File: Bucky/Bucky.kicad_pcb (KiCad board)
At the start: 2 copper layers, 75 x 44.5 mm, 27 parts, among them J1 XT60PW-M, J10 XT30AW-M, J11 XT30AW-M, J12 XT30AW-M, J13 XT30AW-M, J14 XT30AW-M, J2 XT60PW-M, J3 XT30PW-M, J4 XT30PW-M, J5 XT30PW-M, J6 XT30PW-M, J7 XT30AW-M, J8 XT30AW-M, J9 XT30AW-M

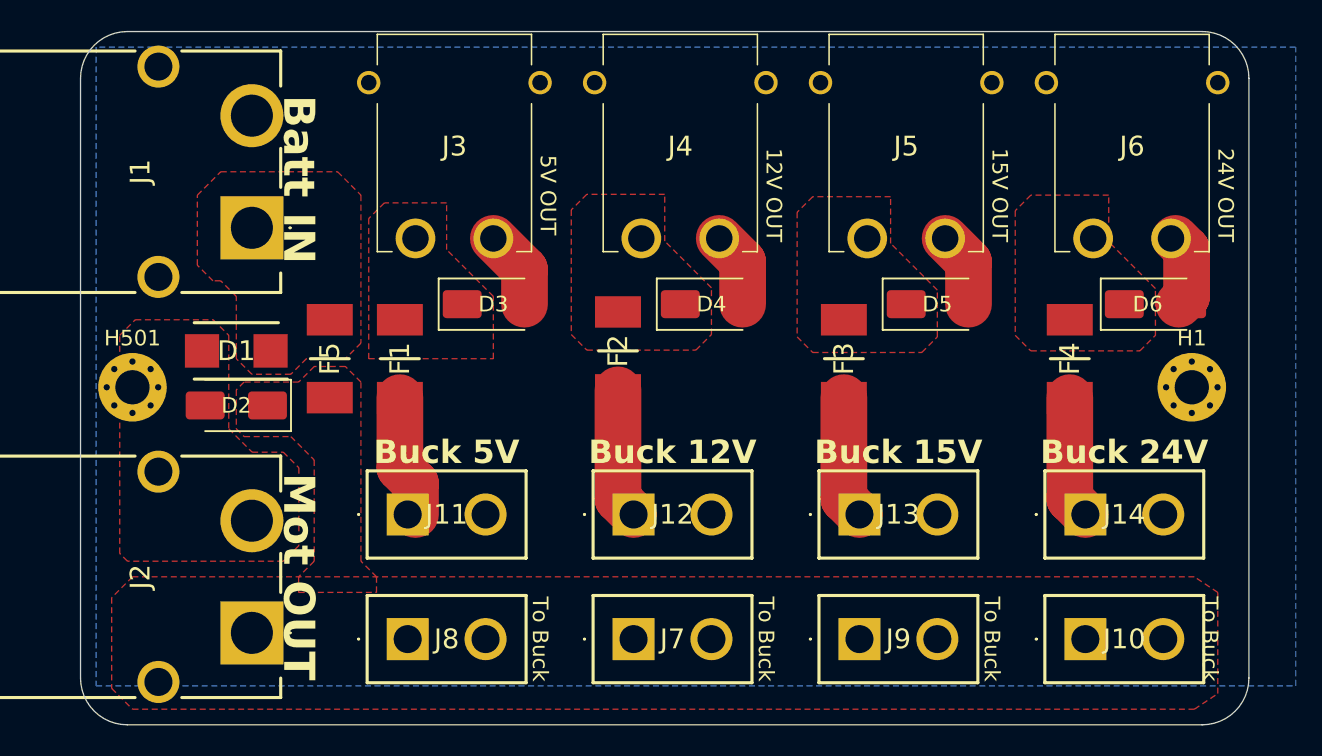
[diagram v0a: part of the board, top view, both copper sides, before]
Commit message: fixed xt60 polarity connection
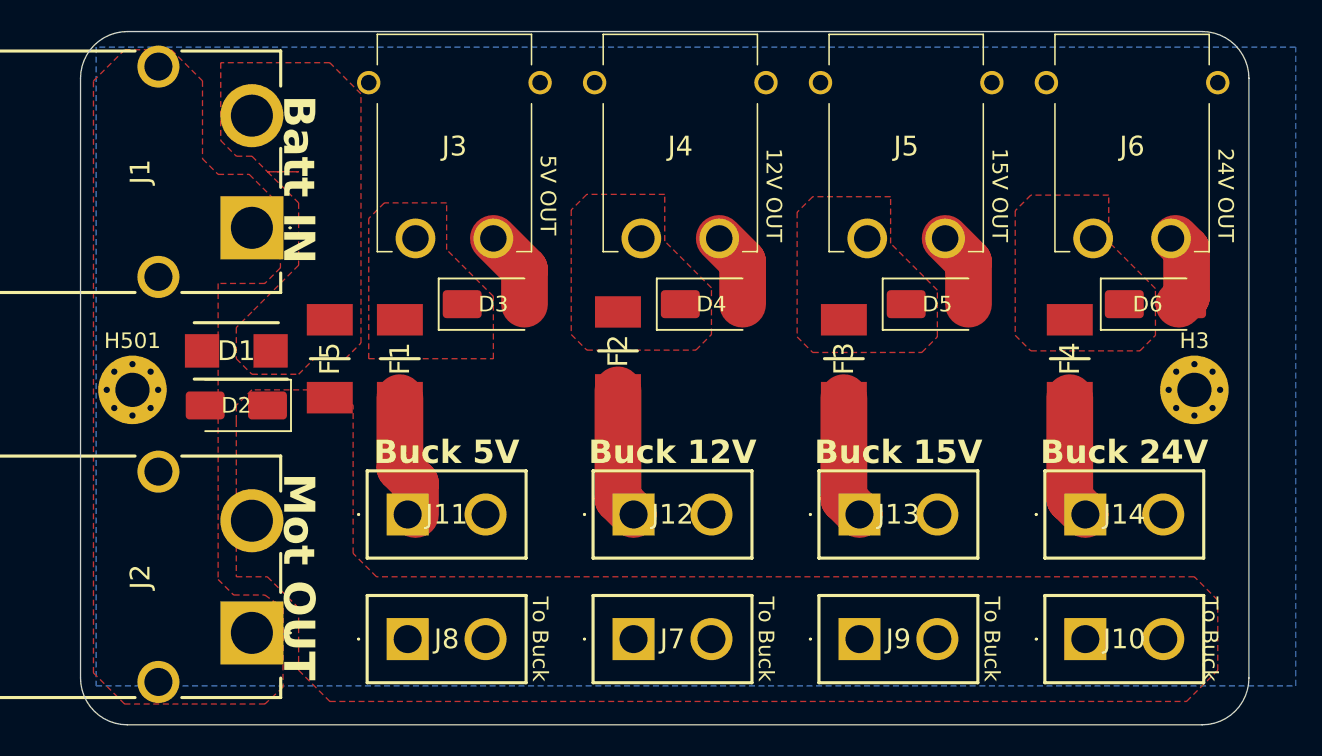
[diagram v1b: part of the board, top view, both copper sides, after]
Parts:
- removed H1: M2 (3.2mm), MountingHole:MountingHole_2.2mm_M2_Pad_Via
- added H3: M2 (3.2mm), MountingHole:MountingHole_2.2mm_M2_Pad_Via, F.Cu at (131.5, 89.0)
- F5: value 0451020.MRL -> 0451015.MRL
- moved H501 0.17 mm to (63.3, 89.0)
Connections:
- F1 pad 1: /Vout5V -> /Vout_5V
- F2 pad 1: /Vout12V -> /Vout_12V
- F3 pad 1: /Vout15V -> /Vout_15V
- F4 pad 1: /Vout24V -> /Vout_24V
- J1 pad 1: /VBatt_in -> GND
- J1 pad 2: GND -> /VBatt_in
- J2 pad 1: /VBuck_in -> GND
- J2 pad 2: GND -> /VBuck_in

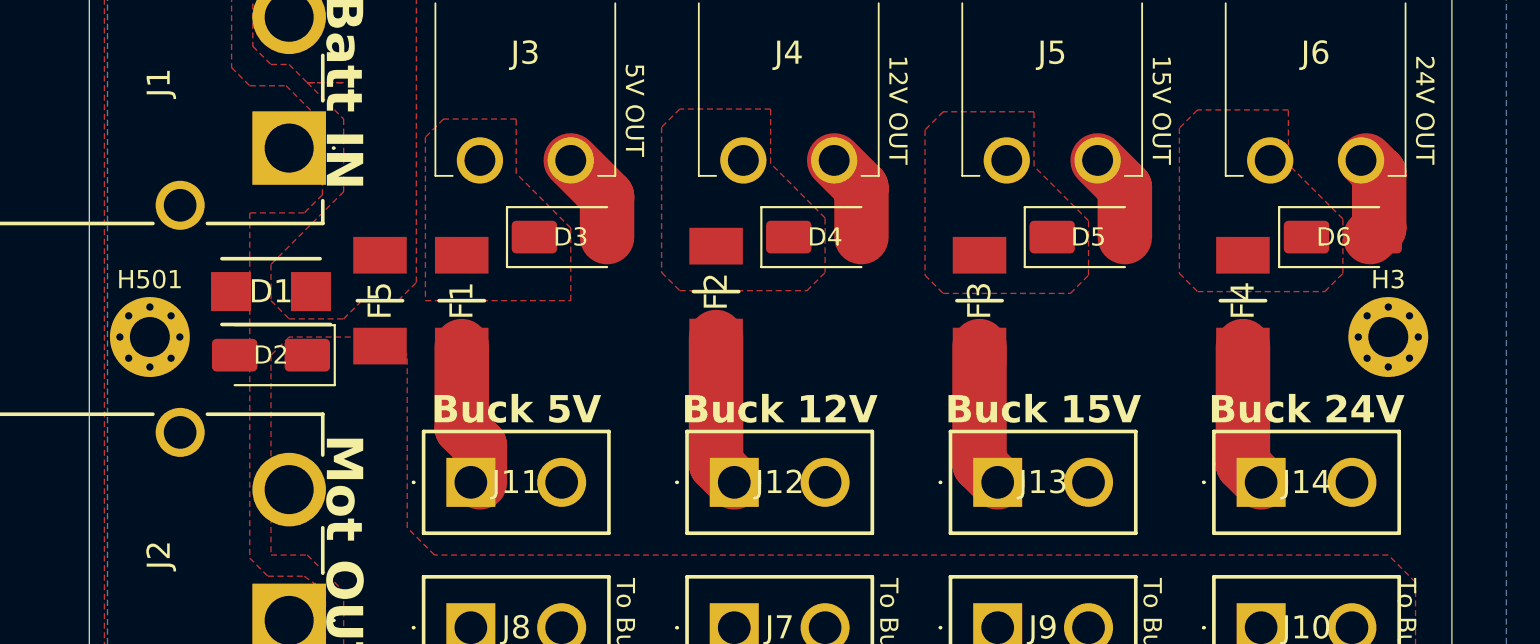
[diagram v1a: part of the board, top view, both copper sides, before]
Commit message: spaced vertical connectors, added 40A fuse
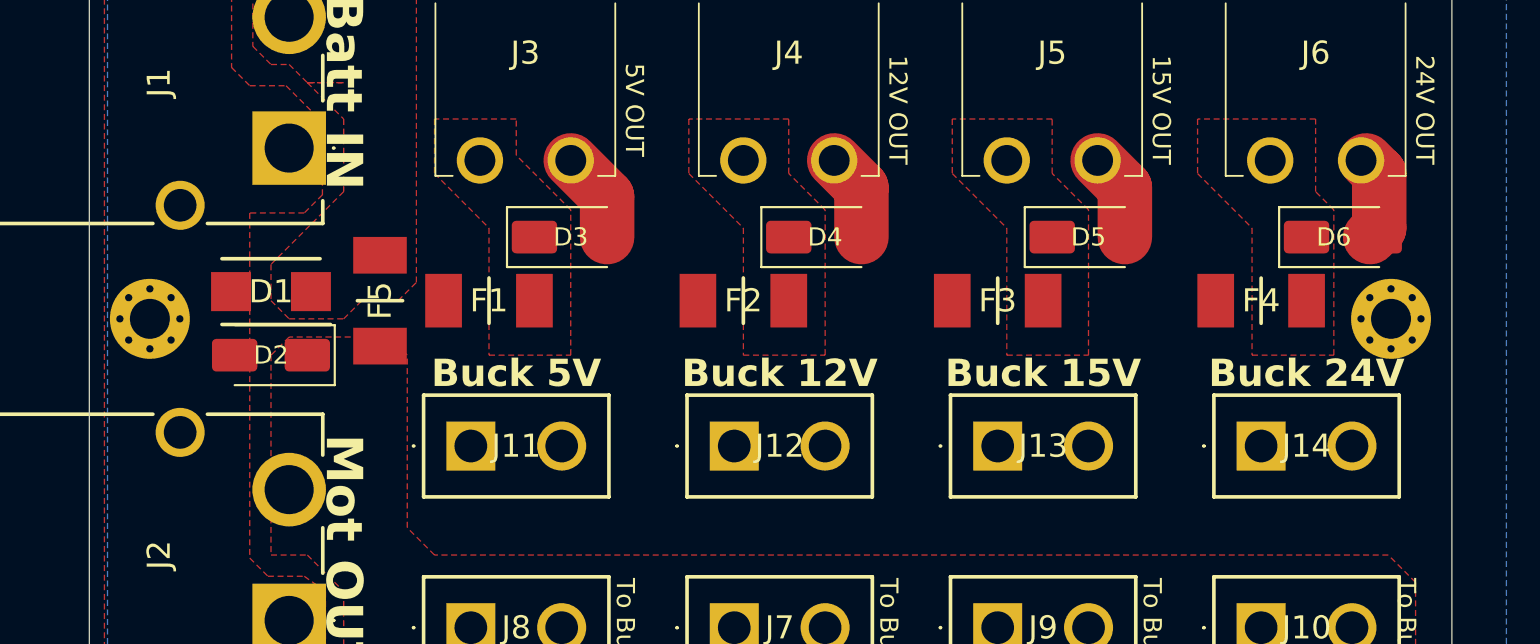
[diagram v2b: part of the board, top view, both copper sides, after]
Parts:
- moved J11 2.00 mm to (81.0, 95.0)
- moved J12 2.00 mm to (95.5, 95.0)
- moved J13 2.00 mm to (110.0, 95.0)
- moved J14 2.00 mm to (124.5, 95.0)
- moved F2 1.58 mm to (96.0, 87.0), turned to 180 degrees
- moved F1 1.50 mm to (82.0, 87.0), turned to 180 degrees
- moved H3 1.01 mm to (131.7, 88.0)
- moved F3 1.00 mm to (110.0, 87.0), turned to 180 degrees
- moved F4 1.00 mm to (124.5, 87.0), turned to 180 degrees
- moved H501 1.00 mm to (63.3, 88.0)
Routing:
- net Net-(F2-Pad2): track 8.41 -> 0.00 mm
- net Net-(F4-Pad2): track 7.91 -> 0.00 mm
- net Net-(F3-Pad2): track 7.91 -> 0.00 mm
- net Net-(F1-Pad2): track 7.91 -> 0.00 mm

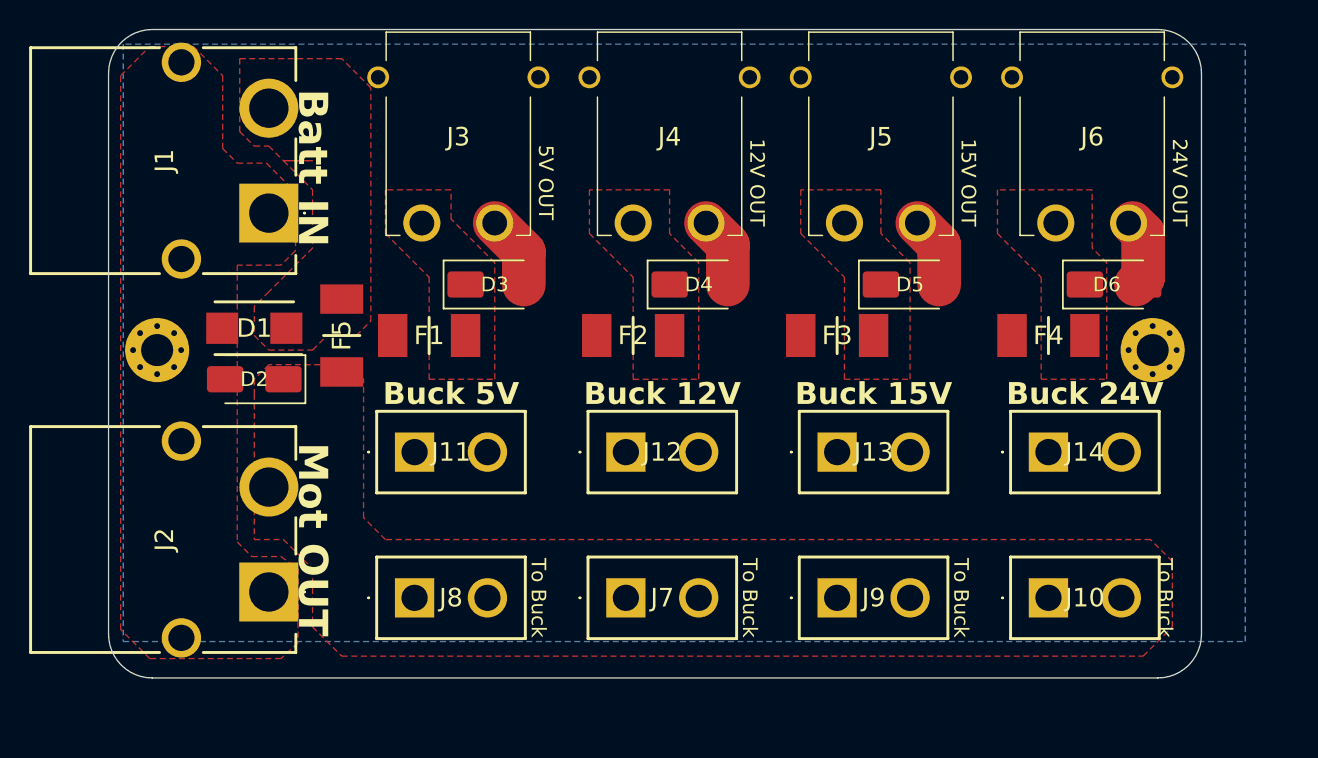
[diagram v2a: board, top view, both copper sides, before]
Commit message: added 4 screws, switched motout and batt in
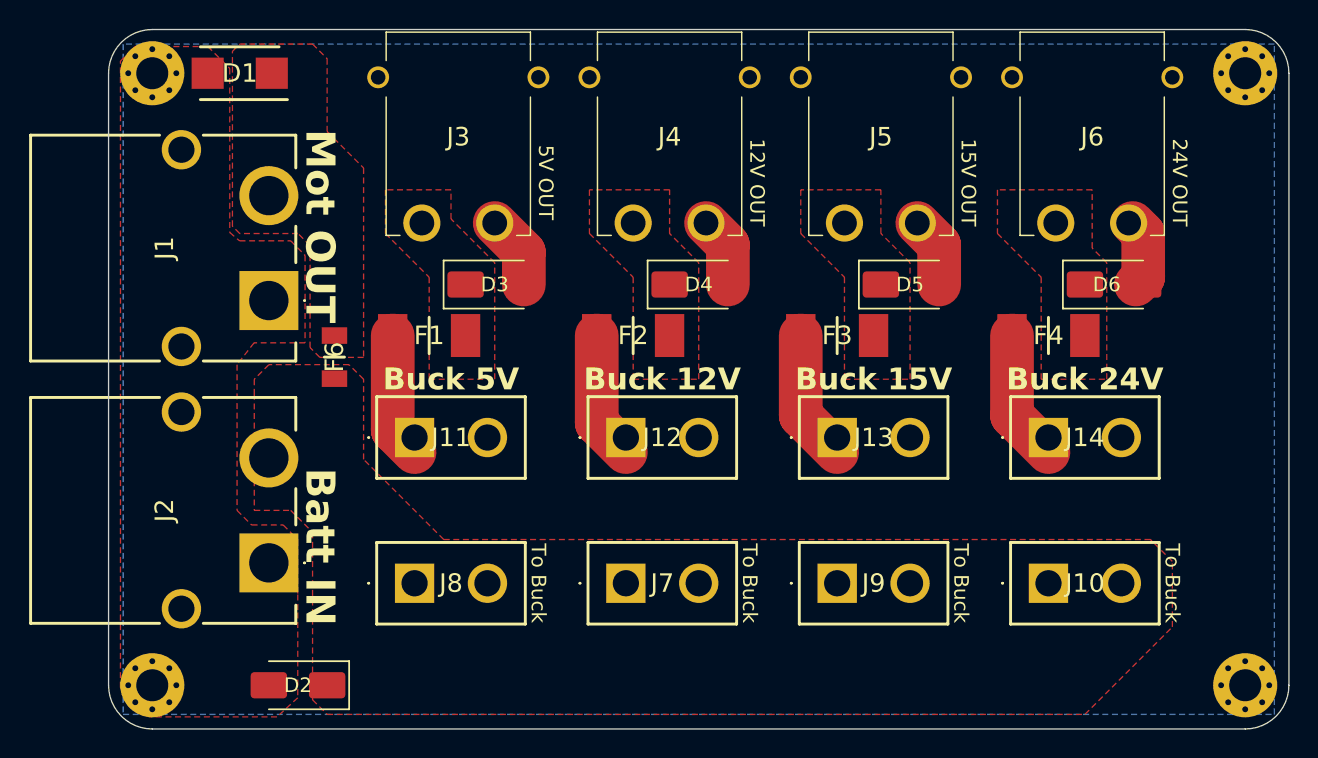
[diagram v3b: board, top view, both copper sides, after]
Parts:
- removed F5: 0451015.MRL, SamacSys_Parts:FUSC6127X294N
- added F6: 0806040.WR, SamacSys_Parts:FUSC3216X110N, F.Cu at (75.5, 88.5)
- added H1: M2 (3.2mm), MountingHole:MountingHole_2.2mm_M2_Pad_Via, F.Cu at (63.0, 111.0)
- added H2: M2 (3.2mm), MountingHole:MountingHole_2.2mm_M2_Pad_Via, F.Cu at (138.0, 111.0)
- moved D2 21.2 mm to (73.0, 111.0)
- moved H3 20.0 mm to (138.0, 69.0)
- moved H501 19.0 mm to (63.0, 69.0)
- moved D1 17.5 mm to (69.0, 69.0)
- moved J1 6.00 mm to (71.0, 84.6)
- moved J2 2.00 mm to (71.0, 102.6)
- moved J10 1.00 mm to (124.5, 104.0)
- moved J11 1.00 mm to (81.0, 94.0)
- moved J12 1.00 mm to (95.5, 94.0)
- moved J13 1.00 mm to (110.0, 94.0)
- moved J14 1.00 mm to (124.5, 94.0)
- moved J7 1.00 mm to (95.5, 104.0)
- moved J8 1.00 mm to (81.0, 104.0)
- moved J9 1.00 mm to (110.0, 104.0)
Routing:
- net Net-(F4-Pad2): track 0.00 -> 9.04 mm
- net Net-(F3-Pad2): track 0.00 -> 9.04 mm
- net Net-(F2-Pad2): track 0.00 -> 8.83 mm
- net Net-(F1-Pad2): track 0.00 -> 8.62 mm
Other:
- board size 75 x 44.5 mm -> 81 x 48 mm
